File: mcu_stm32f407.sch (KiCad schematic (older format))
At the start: 23 parts, among them J1 Conn_01x05_Male, U1 STM32F407VGTx, Y1 8MHz

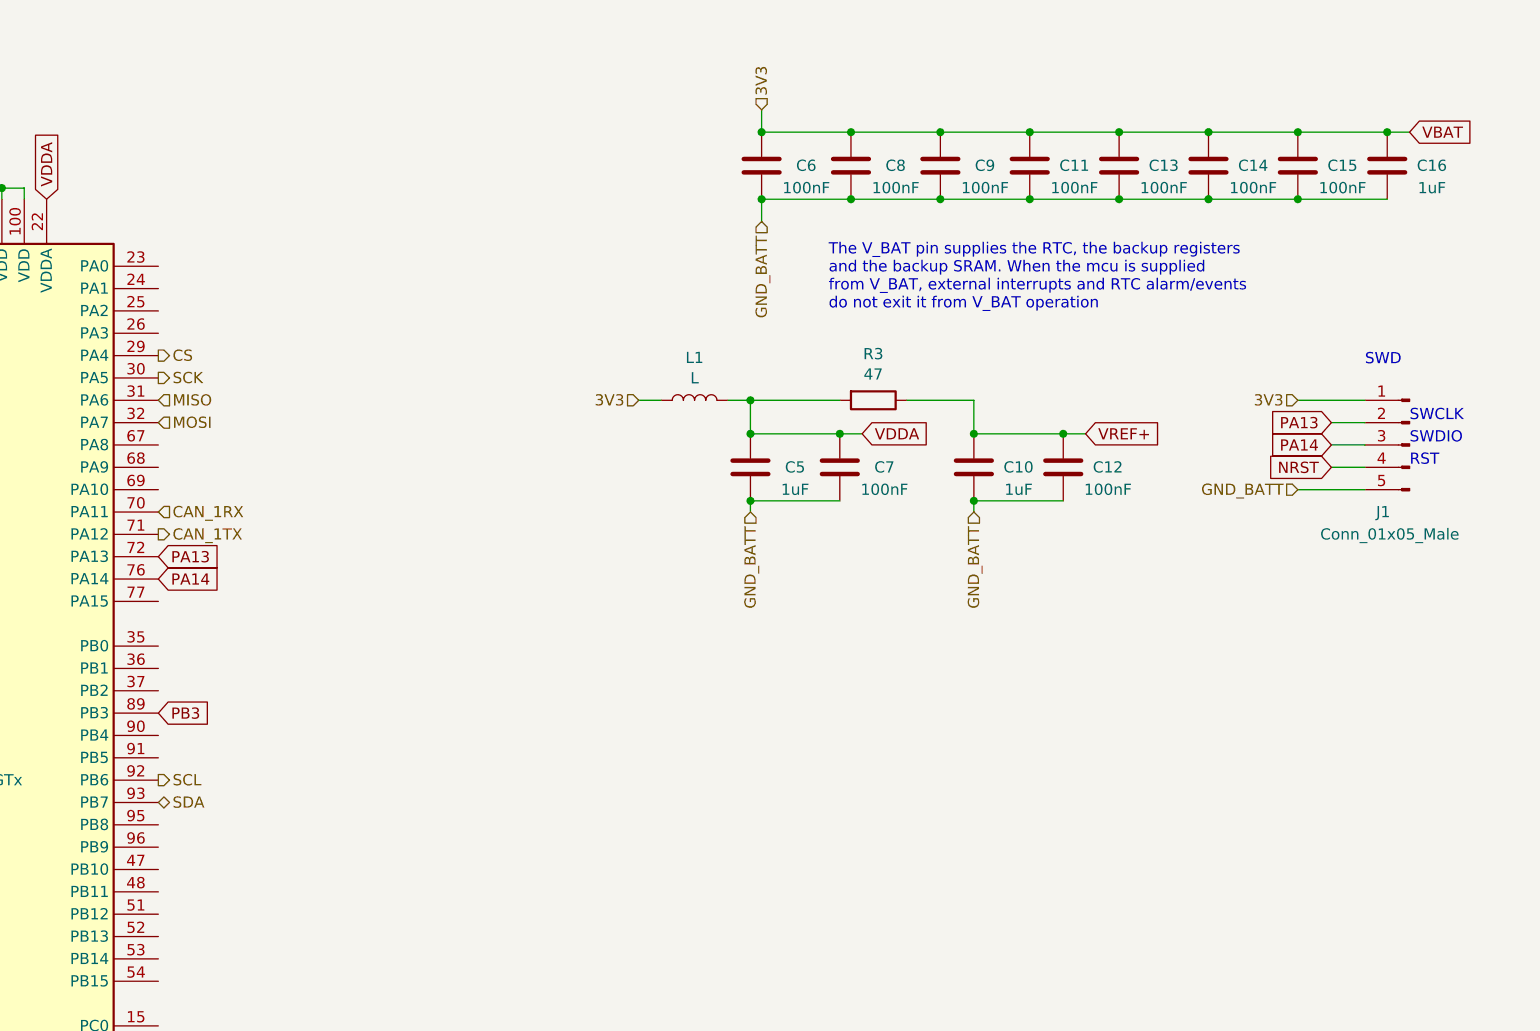
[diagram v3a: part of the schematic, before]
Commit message: Add explanations of Vdd filters
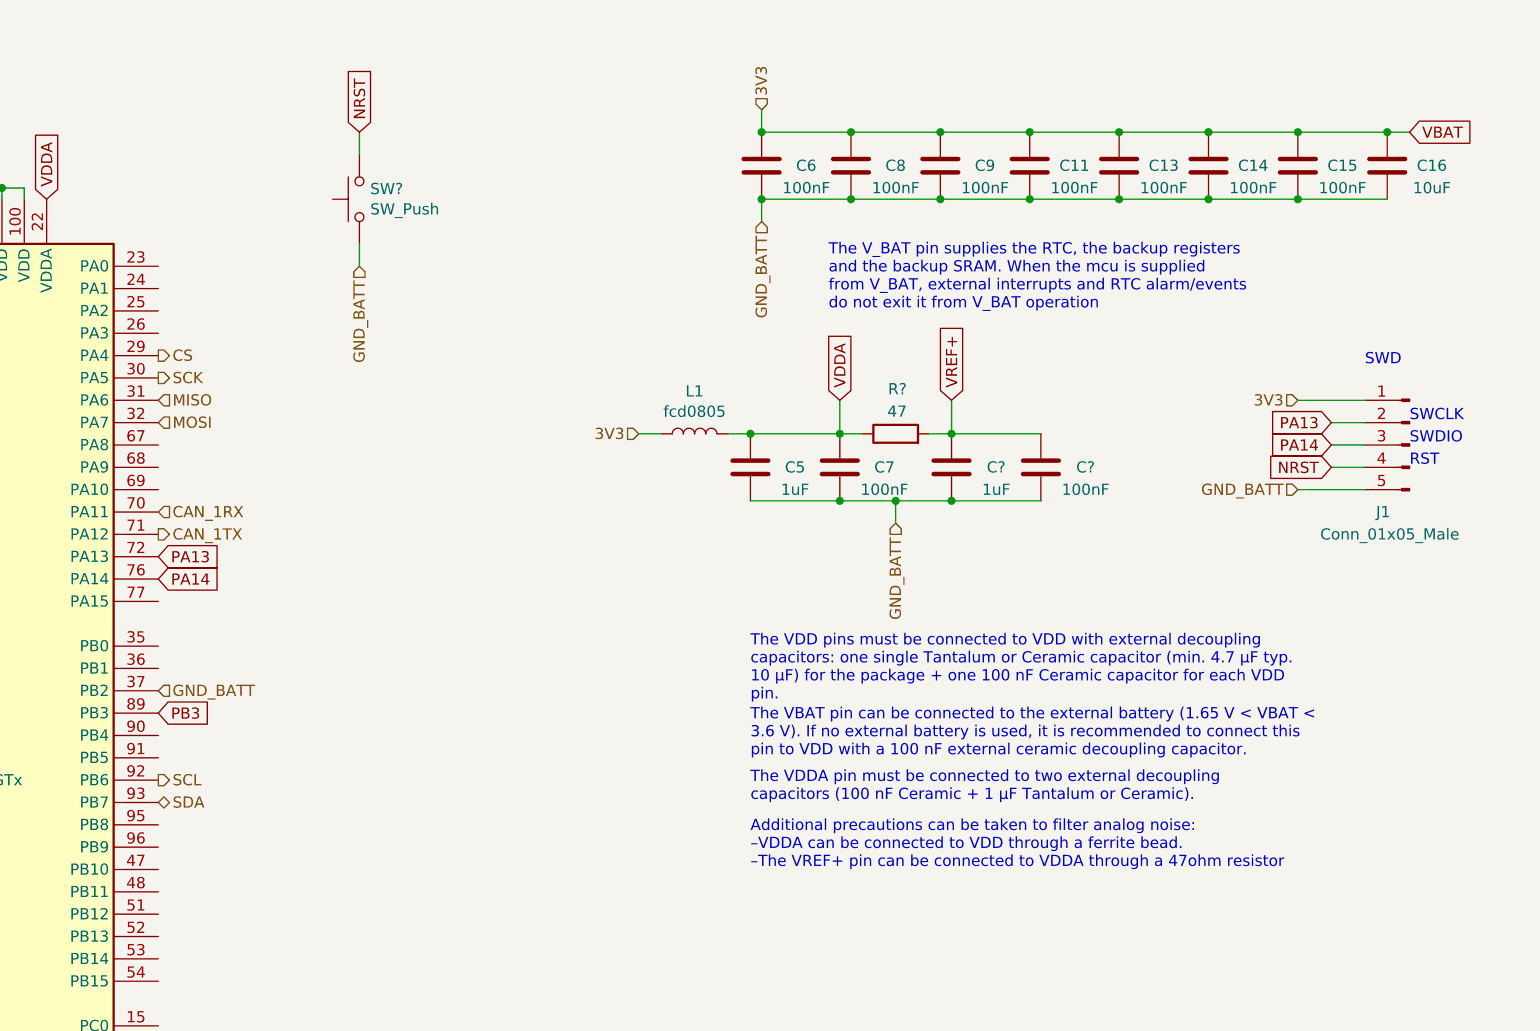
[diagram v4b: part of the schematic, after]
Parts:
- removed C10: 1uF, Capacitor_SMD:C_0805_2012Metric_Pad1.18x1.45mm_HandSolder, symbol Device:C
- removed C12: 100nF, Capacitor_SMD:C_0805_2012Metric_Pad1.18x1.45mm_HandSolder, symbol Device:C
- removed R3: 47, Resistor_SMD:R_0805_2012Metric_Pad1.20x1.40mm_HandSolder, symbol Device:R
- added C?: 1uF, Capacitor_SMD:C_0805_2012Metric_Pad1.18x1.45mm_HandSolder, symbol Device:C
- added C?: 100nF, Capacitor_SMD:C_0805_2012Metric_Pad1.18x1.45mm_HandSolder, symbol Device:C
- added R?: 47, symbol Device:R
- added SW?: SW_Push, symbol Switch:SW_Push
- C16: value 1uF -> 10uF
- L1: value L -> fcd0805
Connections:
- net GND_BATT: now also U1.37 (PB2), C?.2, C?.2, SW?.1
- net NRST: now also SW?.2
- net VDDA: now also R?.1
- net VREF+: now also C?.1, C?.1, R?.2
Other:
- note added: "Additional precautions can be taken to filter analog noise:\n–VDDA can be connected to VDD through a ferrite bead.\n–The VREF+ pin can be connected to VDDA through a 47ohm resistor"
- note added: "The VBAT pin can be connected to the external battery (1.65 V < VBAT <\n3.6 V). If no external battery is used, it is recommended to connect this\npin to VDD with a 100 nF external ceramic decoupling capacitor."
- note added: "The VDD pins must be connected to VDD with external decoupling\ncapacitors: one single Tantalum or Ceramic capacitor (min. 4.7 μF typ.\n10 μF) for the package + one 100 nF Ceramic capacitor for each VDD\npin."
- note added: "The VDDA pin must be connected to two external decoupling\ncapacitors (100 nF Ceramic + 1 μF Tantalum or Ceramic)."
- moved on the sheet: L1
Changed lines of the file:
@@
 	1    0    0    -1
 $EndComp
-Text GLabel 2900 2200 0    50   Input ~ 0
-VREF+
 Wire Wire Line
 	3850 1300 3850 1250
@@
 P 10450 1150
 F 0 "C16" H 10650 1150 50  0000 C CNN
-F 1 "1uF" H 10650 1050 50  0000 C CNN
+F 1 "10uF" H 10650 1050 50  0000 C CNN
 F 2 "Capacitor_SMD:C_0805_2012Metric_Pad1.18x1.45mm_HandSolder" H 10488 1000 50  0001 C CNN
 F 3 "~" H 10450 1150 50  0001 C CNN
@@
 Text GLabel 4450 1300 1    50   Input ~ 0
 VDDA
-Text GLabel 8100 2350 2    50   Input ~ 0
-VDDA
 $Comp
 L Device:C C5
@@
 $EndComp
 Wire Wire Line
-	7100 2200 7200 2200
+	7100 2350 7200 2350
 Wire Wire Line
 	7600 2350 8000 2350
 Wire Wire Line
 	7600 2650 8000 2650
-Wire Wire Line
-	7600 2650 7600 2700
-Connection ~ 7600 2650
 Wire Wire Line
 	8000 2350 8100 2350
 Connection ~ 8000 2350
-Text GLabel 9100 2350 2    50   Input ~ 0
-VREF+
-$Comp
-L Device:C C10
-U 1 1 5FEC05C9
-P 8600 2500
-F 0 "C10" H 8800 2500 50  0000 C CNN
-F 1 "1uF" H 8800 2400 50  0000 C CNN
-F 2 "Capacitor_SMD:C_0805_2012Metric_Pad1.18x1.45mm_HandSolder" H 8638 2350 50  0001 C CNN
-F 3 "~" H 8600 2500 50  0001 C CNN
-	1    8600 2500
-	1    0    0    -1
-$EndComp
-$Comp
-L Device:C C12
-U 1 1 5FEC05CF
-P 9000 2500
-F 0 "C12" H 9200 2500 50  0000 C CNN
-F 1 "100nF" H 9200 2400 50  0000 C CNN
-F 2 "Capacitor_SMD:C_0805_2012Metric_Pad1.18x1.45mm_HandSolder" H 9038 2350 50  0001 C CNN
-F 3 "~" H 9000 2500 50  0001 C CNN
-	1    9000 2500
-	1    0    0    -1
-$EndComp
-Wire Wire Line
-	8600 2350 9000 2350
-Wire Wire Line
-	8600 2650 9000 2650
-Wire Wire Line
-	8600 2650 8600 2700
-Connection ~ 8600 2650
-Wire Wire Line
-	9000 2350 9100 2350
-Connection ~ 9000 2350
 Text Notes 550  900  0    50   ~ 0
 BOOT pins configuration\nBOOT 0    BOOT 1     MODE\n0          X           Main flash memory boot <- Selected\n1          0           System Memory boot (boot loader)\n1          1           RAM memory
@@
 L Device:L L1
 U 1 1 5FEED219
-P 7350 2200
-F 0 "L1" V 7540 2200 50  0000 C CNN
-F 1 "L" V 7449 2200 50  0000 C CNN
-F 2 "Inductor_SMD:L_0805_2012Metric_Pad1.05x1.20mm_HandSolder" H 7350 2200 50  0001 C CNN
-F 3 "~" H 7350 2200 50  0001 C CNN
-	1    7350 2200
+P 7350 2350
+F 0 "L1" V 7540 2350 50  0000 C CNN
+F 1 "fcd0805" V 7449 2350 50  0000 C CNN
+F 2 "Inductor_SMD:L_0805_2012Metric_Pad1.05x1.20mm_HandSolder" H 7350 2350 50  0001 C CNN
+F 3 "https://ar.mouser.com/ProductDetail/Fair-Rite/2508052217Y3/?qs=sGAEpiMZZMukHu%252BjC5l7YT5uox2dNmEjrHrhpdkzVxY%3D" H 7350 2350 50  0001 C CNN
+	1    7350 2350
 	0    -1   -1   0
 $EndComp
-$Comp
-L Device:R R3
-U 1 1 5FEEDA9B
-P 8150 2200
-F 0 "R3" V 7943 2200 50  0000 C CNN
-F 1 "47" V 8034 2200 50  0000 C CNN
-F 2 "Resistor_SMD:R_0805_2012Metric_Pad1.20x1.40mm_HandSolder" V 8080 2200 50  0001 C CNN
-F 3 "~" H 8150 2200 50  0001 C CNN
-	1    8150 2200
-	0    1    1    0
-$EndComp
-Wire Wire Line
-	7500 2200 7600 2200
-Wire Wire Line
-	8600 2200 8600 2350
-Connection ~ 8600 2350
-Wire Wire Line
-	7600 2200 7600 2350
-Connection ~ 7600 2200
-Connection ~ 7600 2350
-Wire Wire Line
-	7600 2200 8000 2200
-Wire Wire Line
-	8600 2200 8300 2200
 Text GLabel 4950 2900 2    50   Input ~ 0
 PA13
@@
 Text HLabel 4050 6950 3    50   Input ~ 0
 GND_BATT
-Text HLabel 7600 2700 3    50   Input ~ 0
-GND_BATT
-Text HLabel 8600 2700 3    50   Input ~ 0
+Text HLabel 8250 2750 3    50   Input ~ 0
 GND_BATT
 Text HLabel 10050 2600 0    50   Input ~ 0
@@
 Text HLabel 7650 900  1    50   Input ~ 0
 3V3
-Text HLabel 7100 2200 0    50   Input ~ 0
+Text HLabel 7100 2350 0    50   Input ~ 0
 3V3
 Text HLabel 3050 1150 1    50   Input ~ 0
@@
 Text HLabel 4950 2800 2    50   Output ~ 0
 CAN_1TX
+Text HLabel 4950 3500 2    50   Input ~ 0
+GND_BATT
+$Comp
+L Switch:SW_Push SW?
+U 1 1 6020B6D3
+P 5850 1300
+F 0 "SW?" V 5896 1252 50  0000 R CNN
+F 1 "SW_Push" V 5805 1252 50  0000 R CNN
+F 2 "" H 5850 1500 50  0001 C CNN
+F 3 "~" H 5850 1500 50  0001 C CNN
+	1    5850 1300
+	0    -1   -1   0
+$EndComp
+Text GLabel 5850 1000 1    50   Input ~ 0
+NRST
+Wire Wire Line
+	5850 1000 5850 1100
+Text HLabel 5850 1600 3    50   Input ~ 0
+GND_BATT
+Wire Wire Line
+	5850 1500 5850 1600
+Text Notes 7600 3550 0    50   ~ 0
+The VDD pins must be connected to VDD with external decoupling\ncapacitors: one single Tantalum or Ceramic capacitor (min. 4.7 μF typ.\n10 μF) for the package + one 100 nF Ceramic capacitor for each VDD\npin.
+Text Notes 7600 3800 0    50   ~ 0
+The VBAT pin can be connected to the external battery (1.65 V < VBAT <\n3.6 V). If no external battery is used, it is recommended to connect this\npin to VDD with a 100 nF external ceramic decoupling capacitor.
+Text Notes 7600 4000 0    50   ~ 0
+The VDDA pin must be connected to two external decoupling\ncapacitors (100 nF Ceramic + 1 μF Tantalum or Ceramic).
+Text GLabel 2900 2200 0    50   Input ~ 0
+VREF+
+$Comp
+L Device:R R?
+U 1 1 6023C24E
+P 8250 2350
+F 0 "R?" V 8450 2300 50  0000 L CNN
+F 1 "47" V 8350 2300 50  0000 L CNN
+F 2 "" V 8180 2350 50  0001 C CNN
+F 3 "~" H 8250 2350 50  0001 C CNN
+	1    8250 2350
+	0    -1   -1   0
+$EndComp
+Text GLabel 8000 2200 1    50   Input ~ 0
+VDDA
+Wire Wire Line
+	8000 2200 8000 2350
+Text GLabel 8500 2200 1    50   Input ~ 0
+VREF+
+Wire Wire Line
+	8500 2350 8400 2350
+$Comp
+L Device:C C?
+U 1 1 60267A98
+P 8500 2500
+F 0 "C?" H 8700 2500 50  0000 C CNN
+F 1 "1uF" H 8700 2400 50  0000 C CNN
+F 2 "Capacitor_SMD:C_0805_2012Metric_Pad1.18x1.45mm_HandSolder" H 8538 2350 50  0001 C CNN
+F 3 "~" H 8500 2500 50  0001 C CNN
+	1    8500 2500
+	1    0    0    -1
+$EndComp
+Wire Wire Line
+	8500 2350 8900 2350
+Connection ~ 8500 2350
+Connection ~ 8000 2650
+Connection ~ 8500 2650
+Wire Wire Line
+	8500 2650 8900 2650
+Wire Wire Line
+	8000 2650 8250 2650
+Wire Wire Line
+	8250 2650 8250 2750
+Connection ~ 8250 2650
+Wire Wire Line
+	8250 2650 8500 2650
+Wire Wire Line
+	7500 2350 7600 2350
+Connection ~ 7600 2350
+$Comp
+L Device:C C?
+U 1 1 60267A9E
+P 8900 2500
+F 0 "C?" H 9100 2500 50  0000 C CNN
+F 1 "100nF" H 9100 2400 50  0000 C CNN
+F 2 "Capacitor_SMD:C_0805_2012Metric_Pad1.18x1.45mm_HandSolder" H 8938 2350 50  0001 C CNN
+F 3 "~" H 8900 2500 50  0001 C CNN
+	1    8900 2500
+	1    0    0    -1
+$EndComp
+Wire Wire Line
+	8500 2200 8500 2350
+Text Notes 7600 4300 0    50   ~ 0
+Additional precautions can be taken to filter analog noise:\n–VDDA can be connected to VDD through a ferrite bead.\n–The VREF+ pin can be connected to VDDA through a 47ohm resistor
 $EndSCHEMATC
